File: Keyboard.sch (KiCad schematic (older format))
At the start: 1 part

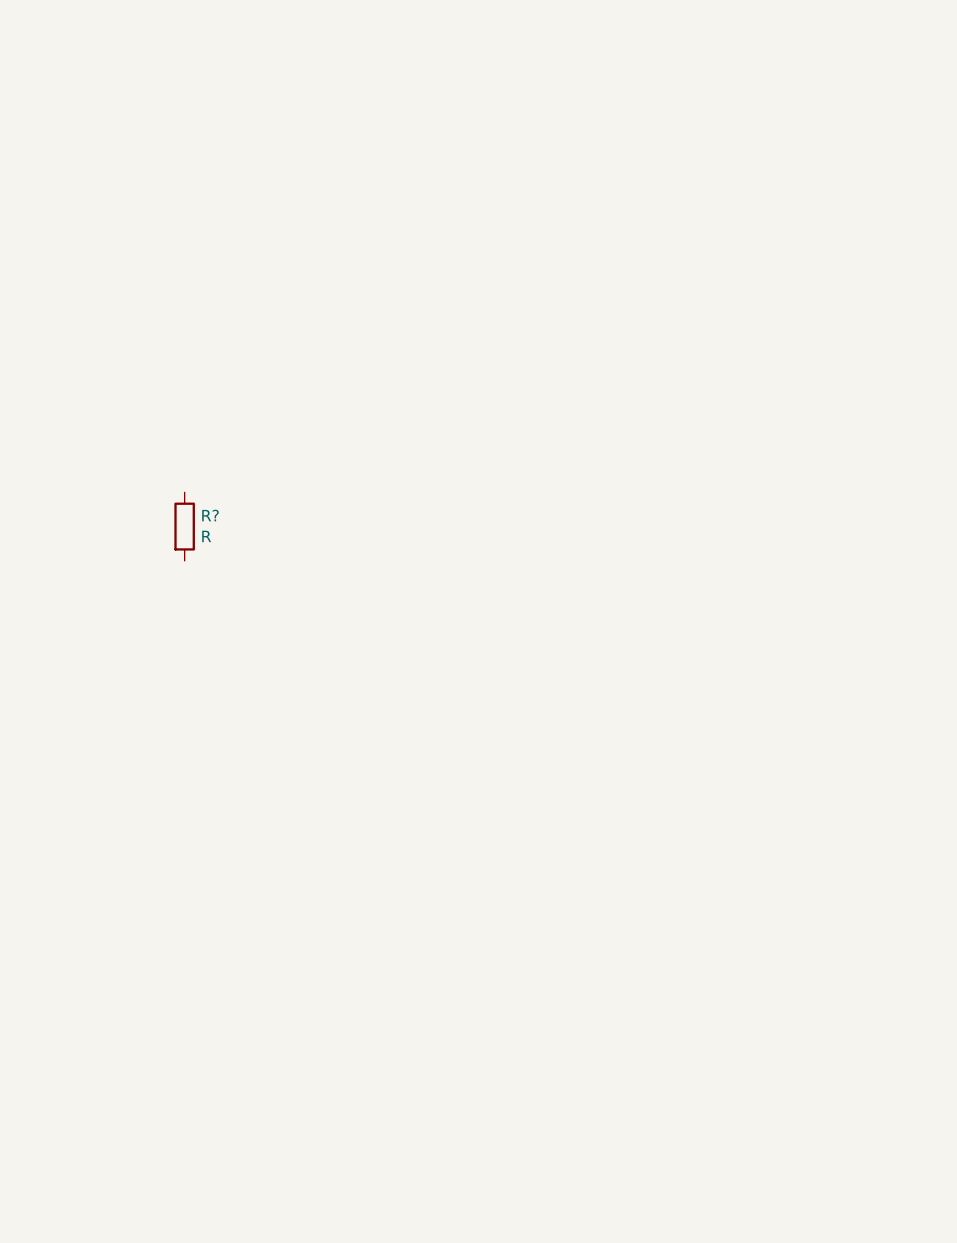
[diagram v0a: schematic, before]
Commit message: SCHEMATIC FOR THE KEYBOARD ATMEGA32 MCU
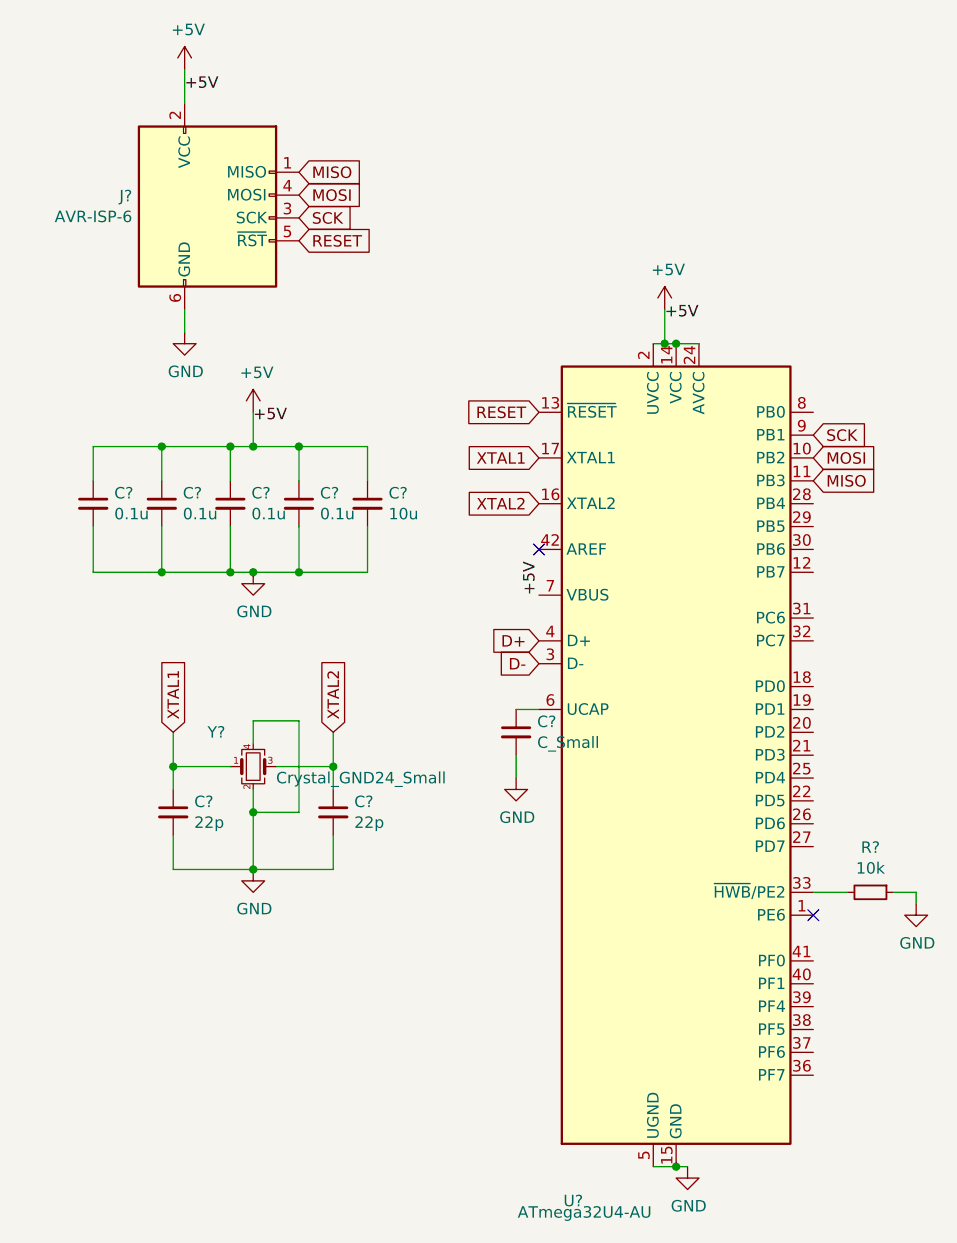
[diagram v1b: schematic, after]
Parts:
- removed R?: R, symbol Device:R
- added C?: C_Small, symbol Device:C_Small
- added C? (x2): 22p, symbol Device:C_Small
- added C? (x4): 0.1u, symbol Device:C_Small
- added C?: 10u, symbol Device:C_Small
- added J?: AVR-ISP-6, symbol Connector:AVR-ISP-6
- added R?: 10k, symbol Device:R_Small
- added U?: ATmega32U4-AU, Package_QFP:TQFP-44_10x10mm_P0.8mm, symbol MCU_Microchip_ATmega:ATmega32U4-AU
- added Y?: Crystal_GND24_Small, symbol Device:Crystal_GND24_Small
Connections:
- new net: R?.2, U?.33 (~HWB~/PE2)
- new net: C?.1, U?.6 (UCAP)
- new net +5V: C?.1, C?.1, C?.1, C?.1, C?.1, J?.2 (VCC), U?.14 (VCC), U?.2 (UVCC), U?.24 (AVCC), U?.34 (VCC), U?.44 (AVCC), U?.7 (VBUS)
- new net D+: U?.4 (D+)
- new net D-: U?.3 (D-)
- new net GND: C?.2, C?.2, C?.2, C?.2, C?.2, C?.2, C?.2, C?.2, J?.6 (GND), R?.1, U?.15 (GND), U?.23 (GND), U?.35 (GND), U?.43 (GND), U?.5 (UGND), Y?.2, Y?.4
- new net MISO: J?.1 (MISO), U?.11 (PB3)
- new net MOSI: J?.4 (MOSI), U?.10 (PB2)
- new net RESET: J?.5 (~RST), U?.13 (~RESET)
- new net SCK: J?.3 (SCK), U?.9 (PB1)
- new net XTAL1: C?.1, U?.17 (XTAL1), Y?.1
- new net XTAL2: C?.1, U?.16 (XTAL2), Y?.3
- no-connect marks 0 -> 2
